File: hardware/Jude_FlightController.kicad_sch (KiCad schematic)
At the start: 0 parts

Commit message: updated schematic with wiring for IMU, barometer, SD, and voltage converter
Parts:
- added C1, C2: 100nF, Capacitor_SMD:C_01005_0402Metric, symbol Device:C
- added C3, C4: 0.1uF, Capacitor_SMD:C_01005_0402Metric, symbol Device:C
- added Cboot: 0.1uF, Capacitor_SMD:C_0402_1005Metric, symbol Device:C
- added Cin: 2.2uF, Capacitor_SMD:C_0402_1005Metric, symbol Device:C
- added Cout, Cout1: 22uF, Capacitor_SMD:C_0402_1005Metric, symbol Device:C
- added I2CPullupSCL, I2CPullupSDA, R1, R2, R3, R4, R5, R6, R7: 10K, Resistor_SMD:R_01005_0402Metric, symbol Device:R
- added L1: 5.6uH, Inductor_SMD:L_01005_0402Metric, symbol Device:L
- added LED1: YLED0805R, easyeda2kicad:LED0805-R-RD_RED, symbol lcscsymbols:YLED0805R
- added Rfbb: 22K, Resistor_SMD:R_01005_0402Metric, symbol Device:R
- added Rfbt: 100K, Resistor_SMD:R_01005_0402Metric, symbol Device:R
- added U1: BMP580, easyeda2kicad:LGA-10_L2.0-W2.0-P0.50-TL_BMP580, symbol lcscsymbols:BMP580
- added U2: ICM-45686, easyeda2kicad:LGA-14_L3.0-W2.5-P0.50-TL, symbol lcscsymbols:ICM-45686
- added U3: JBL-102010052, easyeda2kicad:TF-CARD-SMD_JBL-102010052, symbol lcscsymbols:JBL-102010052
- added U4: LMR51430XFDDCR, easyeda2kicad:SOT-23-6_L2.9-W1.6-P0.95-LS2.8-BL, symbol lcscsymbols:LMR51430XDDCR
- added U5: QMC5883P, easyeda2kicad:LGA-16_L3.0-W3.0-P0.50-BL_SQ, symbol lcscsymbols:QMC5883P
- added U6: SAM-M10Q-00B, easyeda2kicad:LCC-20_L15.5-W15.5-P1.90_SAM-M10Q-00B, symbol lcscsymbols:SAM-M10Q-00B
- added U7: SN74LVC1G04DBVR, easyeda2kicad:SOT-23-5_L3.0-W1.7-P0.95-LS2.8-BR, symbol lcscsymbols:SN74LVC1G04DBVR
- added U8: STM32F722RET6TR, easyeda2kicad:LQFP-64_L10.0-W10.0-P0.50-LS12.0-BL, symbol lcscsymbols:STM32F722RET6TR
- added USB1: TYPEC-304J-BCP16, easyeda2kicad:USB-C-SMD_TYPEC-304J-BCP16, symbol lcscsymbols:TYPEC-304J-BCP16
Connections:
- new net: Rfbb.1, Rfbt.2, U4.4 (FB)
- new net: Cboot.2, L1.1, U4.2 (SW)
- new net: Cboot.1, U4.6 (CB)
- new net: R6.2, U3.8 (DAT1)
- new net +3.3V: C1.2, C2.1, C3.1, C4.1, Cout.1, Cout1.1, I2CPullupSCL.1, I2CPullupSDA.1, L1.2, R1.1, R2.1, R3.1, R4.1, R5.1, R6.1, R7.1, Rfbt.1, U1.1 (VDDIO), U1.10 (VDD), U2.5 (VDDIO), U2.8 (VDD), U3.4 (VDD)
- new net BMP_INT: U1.7 (INT)
- new net GND: C1.1, C2.2, C3.2, C4.2, U1.3 (VSS), U1.5 (SDO), U1.6 (CSB), U1.8 (VSS), U1.9 (VSS), U2.6 (GND), U3.10 (GND), U3.11 (GND), U3.12 (GND), U3.6 (VSS), U3.9 (GND)
- new net I2C_SCL: I2CPullupSCL.2, U1.2 (SCK)
- new net I2C_SDA: I2CPullupSDA.2, U1.4 (SDI)
- new net ICM_CS: U2.12 (AP_CS)
- new net ICM_INT1: U2.4 (INT1/INT)
- new net ICM_INT2: U2.9 (INT2/FSYNC/CLKIN)
- new net ICM_SCK: U2.13 (AP_SCL/AP_SCLK)
- new net ICM_SDI: U2.14 (AP_SDA/AP_SDIO/AP_SDI)
- new net ICM_SDO: U2.1 (AP_SDO/AP_AD0)
- new net PGND: Cin.2, Cout.2, Cout1.2, Rfbb.2, U4.1 (GND)
- new net SD_CD: R7.2, U3.CD
- new net SD_CLK: R4.2, U3.5 (CLK)
- new net SD_CMD: R3.2, U3.3 (CMD)
- new net SD_DAT0: R5.2, U3.7 (DAT0)
- new net SD_DAT2: R1.2, U3.1 (DAT2)
- new net SD_DAT3: R2.2, U3.2 (CD/DAT3)
- new net VBEC: Cin.1, U4.3 (VIN), U4.5 (EN)
- no-connect marks 0 -> 5

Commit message: ignore .history folder
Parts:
- added C10, C12, C5, C6, C7, C9: 100nF, Capacitor_SMD:C_01005_0402Metric, symbol Device:C
- added C11: 4.7uF, Capacitor_SMD:C_01005_0402Metric, symbol Device:C
- added C8: 10uF, Capacitor_SMD:C_01005_0402Metric, symbol Device:C
- added R12, R13: 10K, Resistor_SMD:R_01005_0402Metric, symbol Device:R
- added R8, R9: 5.1K, Resistor_SMD:R_01005_0402Metric, symbol Device:R
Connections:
- net +3.3V: now also U5.2 (VDD), U6.17 (VCC), U6.2 (V_IO), U6.3 (V_BCKP), U7.5 (VCC), C10.1, C12.1, C5.2, C6.1, C7.1, C8.1, C9.1, R12.1, R13.2
- net GND: now also U5.11 (GND), U5.9 (GND), U6.1 (GND), U6.10 (GND), U6.11 (GND), U6.15 (GND), U6.16 (GND), U6.20 (GND), U6.4 (GND), U6.5 (GND), U6.6 (GND), U7.3 (GND), USB1.13 (GND), USB1.14 (GND), USB1.15 (GND), USB1.16 (GND), USB1.A1B12 (GND), USB1.B1A12 (GND), C10.2, C11.2, C12.2, C5.1, C6.2, C7.2, C8.2, C9.2, R8.1, R9.1
- net I2C_SCL: now also U5.1 (SCK)
- net I2C_SDA: now also U5.16 (SDA)
- net GPS_TX: now reaches U6.13 (TXD)
- net GPS_RX: now reaches U6.14 (RXD)
- net at U6.18 (RESET_N): now also R13.1
- net at U6.8 (SAFEBOOT_N): now also R12.2
- net SBUS_IN: now reaches U7.2 (A)
- net SBUS_INV: now reaches U7.4 (Y)
- net VBUS: now reaches USB1.A4B9 (VBUS)
- net VBUS: now also USB1.B4A9 (VBUS)
- net at USB1.A5 (CC1): now also R9.2
- net USB_DP: now reaches USB1.A6 (DP1)
- net USB_DP: now also USB1.B6 (DP2)
- net USB_DN: now reaches USB1.A7 (DN1)
- net USB_DN: now also USB1.B7 (DN2)
- net at USB1.B5 (CC2): now also R8.2
- net at U5.10 (C1): now also C11.1
- net VBEC renamed +5V
- no-connect marks 5 -> 22
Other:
- moved on the sheet: LED1, U5, U6, U7, U8, USB1

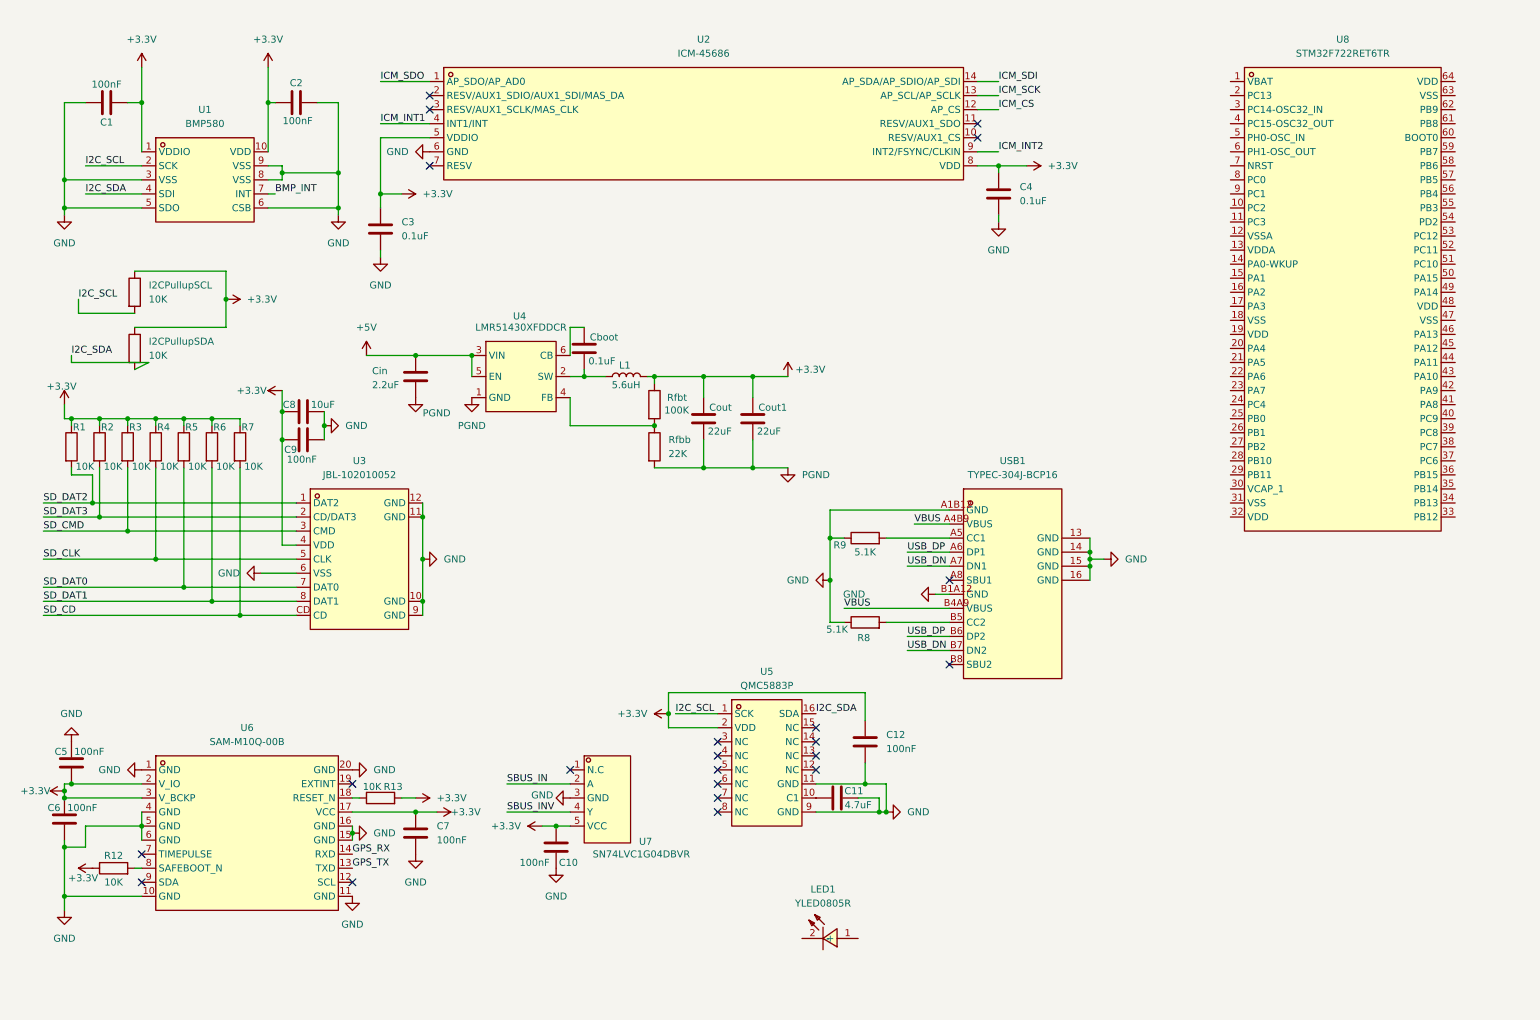
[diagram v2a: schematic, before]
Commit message: finished schematic with microcontroller and all supporting components
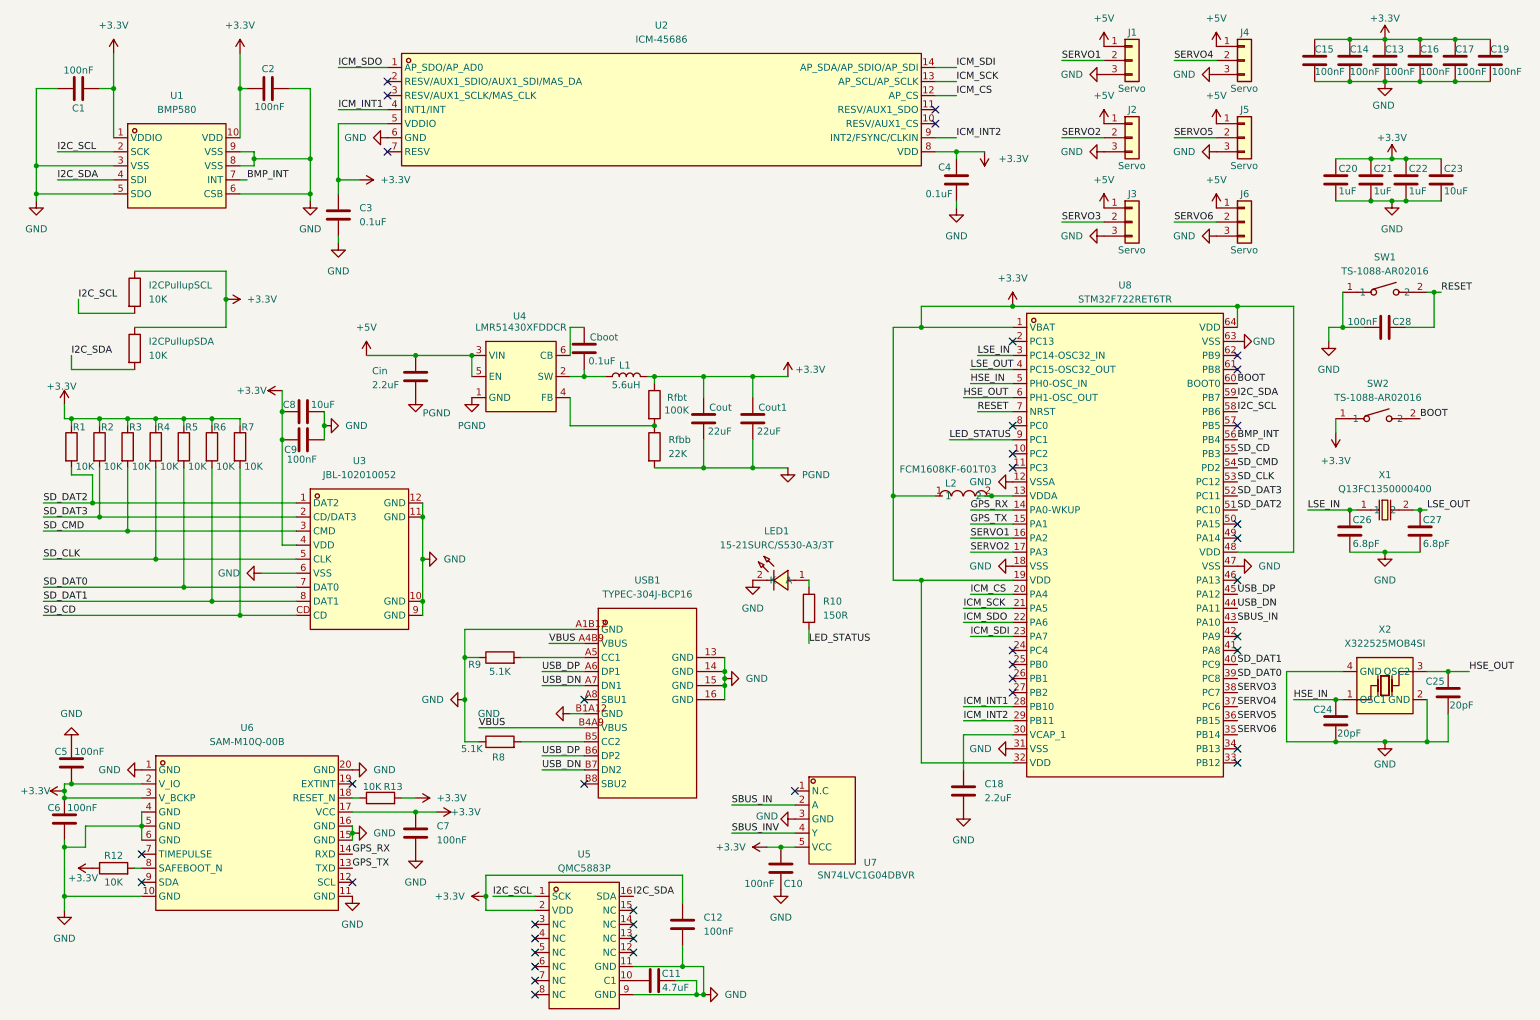
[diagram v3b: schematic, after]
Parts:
- removed LED1: YLED0805R, easyeda2kicad:LED0805-R-RD_RED, symbol lcscsymbols:YLED0805R
- added C13, C14, C15, C16, C17, C19, C28: 100nF, Capacitor_SMD:C_01005_0402Metric, symbol Device:C
- added C18: 2.2uF, Capacitor_SMD:C_01005_0402Metric, symbol Device:C
- added C20, C21, C22: 1uF, Capacitor_SMD:C_01005_0402Metric, symbol Device:C
- added C23: 10uF, Capacitor_SMD:C_01005_0402Metric, symbol Device:C
- added C24, C25: 20pF, Capacitor_SMD:C_01005_0402Metric, symbol Device:C
- added C26, C27: 6.8pF, Capacitor_SMD:C_01005_0402Metric, symbol Device:C
- added J1, J2, J3, J4, J5, J6: Servo, symbol Connector_Generic:Conn_01x03
- added L2: FCM1608KF-601T03, easyeda2kicad:L0603, symbol lcscsymbols:FCM1608KF-601T03
- added LED1: 15-21SURC/S530-A3/3T, easyeda2kicad:LED1206-R-RD_RED, symbol lcscsymbols:15-21SURC_S530-A3_3T
- added R10: 150R, Resistor_SMD:R_01005_0402Metric, symbol Device:R
- added SW1, SW2: TS-1088-AR02016, easyeda2kicad:SW-SMD_L3.9-W3.0-P4.45, symbol lcscsymbols:TS-1088-AR02016
- added X1: Q13FC1350000400, easyeda2kicad:FC-135R_L3.2-W1.5, symbol lcscsymbols:Q13FC1350000400
- added X2: X322525MOB4SI, easyeda2kicad:CRYSTAL-SMD_4P-L3.2-W2.5-BL, symbol lcscsymbols:X322525MOB4SI
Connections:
- net +3.3V: now also U8.1 (VBAT), U8.19 (VDD), U8.32 (VDD), U8.48 (VDD), U8.64 (VDD), C13.1, C14.1, C15.1, C16.1, C17.1, C19.1, C20.1, C21.1, C22.1, C23.1, L2.1, SW2.1
- net +5V: now also J1.1 (Pin_1), J2.1 (Pin_1), J3.1 (Pin_1), J4.1 (Pin_1), J5.1 (Pin_1), J6.1 (Pin_1)
- net BMP_INT: now also U8.56 (PB4)
- net GND: now also U8.12 (VSSA), U8.18 (VSS), U8.31 (VSS), U8.47 (VSS), U8.63 (VSS), C13.2, C14.2, C15.2, C16.2, C17.2, C18.2, C19.2, C20.2, C21.2, C22.2, C23.2, C24.2, C25.2, C26.2, C27.2, C28.1, J1.3 (Pin_3), J2.3 (Pin_3), J3.3 (Pin_3), J4.3 (Pin_3), J5.3 (Pin_3), J6.3 (Pin_3), LED1.2 (K), SW1.1, X2.2 (GND), X2.4 (GND)
- net GPS_RX: now also U8.14 (PA0-WKUP)
- net GPS_TX: now also U8.15 (PA1)
- net I2C_SCL: now also U8.58 (PB6)
- net I2C_SDA: now also U8.59 (PB7)
- net ICM_CS: now also U8.20 (PA4)
- net ICM_INT1: now also U8.28 (PB10)
- net ICM_INT2: now also U8.29 (PB11)
- net ICM_SCK: now also U8.21 (PA5)
- net ICM_SDI: now also U8.23 (PA7)
- net ICM_SDO: now also U8.22 (PA6)
- net SBUS_IN: now also U8.43 (PA10)
- net SD_CD: now also U8.55 (PB3)
- net SD_CLK: now also U8.53 (PC12)
- net SD_CMD: now also U8.54 (PD2)
- net SD_DAT0: now also U8.39 (PC8)
- net SD_DAT2: now also U8.51 (PC10)
- net SD_DAT3: now also U8.52 (PC11)
- net USB_DN: now also U8.44 (PA11)
- net USB_DP: now also U8.45 (PA12)
- net at U8.13 (VDDA): now also L2.2
- net SERVO1: now reaches U8.16 (PA2)
- net SERVO1: now also J1.2 (Pin_2)
- net SERVO2: now reaches U8.17 (PA3)
- net SERVO2: now also J2.2 (Pin_2)
- net LSE_IN: now reaches U8.3 (PC14-OSC32_IN)
- net LSE_IN: now also C26.1, X1.1
- net at U8.30 (VCAP_1): now also C18.1
- net SERVO6: now reaches U8.35 (PB14)
- net SERVO6: now also J6.2 (Pin_2)
- net SERVO5: now reaches U8.36 (PB15)
- net SERVO5: now also J5.2 (Pin_2)
- net SERVO4: now reaches U8.37 (PC6)
- net SERVO4: now also J4.2 (Pin_2)
- net SERVO3: now reaches U8.38 (PC7)
- net SERVO3: now also J3.2 (Pin_2)
- net LSE_OUT: now reaches U8.4 (PC15-OSC32_OUT)
- net LSE_OUT: now also C27.1, X1.2
- net at U8.40 (PC9): no longer names the net of U8.40 (PC9)
- net at U8.40 (PC9): now also R6.2, U3.8 (DAT1)
- net HSE_IN: now reaches U8.5 (PH0-OSC_IN)
- net HSE_IN: now also C24.1, X2.1 (OSC1)
- net HSE_OUT: now reaches U8.6 (PH1-OSC_OUT)
- net HSE_OUT: now also C25.1, X2.3 (OSC2)
- net BOOT: now reaches U8.60 (BOOT0)
- net BOOT: now also SW2.2
- net RESET: now reaches U8.7 (NRST)
- net RESET: now also C28.2, SW1.2
- net LED_STATUS: now reaches U8.9 (PC1)
- net LED_STATUS: now also R10.2
- new net: LED1.1 (A), R10.1
- no-connect marks 22 -> 40
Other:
- company: (none) -> Feldman Dynamics
- title: (none) -> BirdBrainV1
- moved on the sheet: C1, C10, C11, C12, C2, C3, C4, R8, R9, U1, U2, U5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

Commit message: organized schematic
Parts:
- removed C10: 100nF, Capacitor_SMD:C_01005_0402Metric, symbol Device:C
- removed U7: SN74LVC1G04DBVR, easyeda2kicad:SOT-23-5_L3.0-W1.7-P0.95-LS2.8-BR, symbol lcscsymbols:SN74LVC1G04DBVR
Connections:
- no-connect marks 40 -> 39
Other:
- note added: "Barometer"
- note added: "Crystal Oscillators"
- note added: "Decoupling"
- note added: "GPS"
- note added: "I2C Pullups"
- note added: "IMU"
- note added: "Magnetometer"
- note added: "Reset/Boot Buttons"
- note added: "SD Connector"
- note added: "STM32"
- note added: "Servo Headers"
- note added: "Status LED"
- note added: "USB-C Connector"
- note added: "Voltage Converter"
- moved on the sheet: C1, C13, C14, C15, C16, C17, C18, C19, C2, C20, C21, C22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
